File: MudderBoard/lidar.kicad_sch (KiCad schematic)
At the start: 24 parts, among them Q1 NMOS, Q2 NMOS, U1 LM5122QMH/NOPB

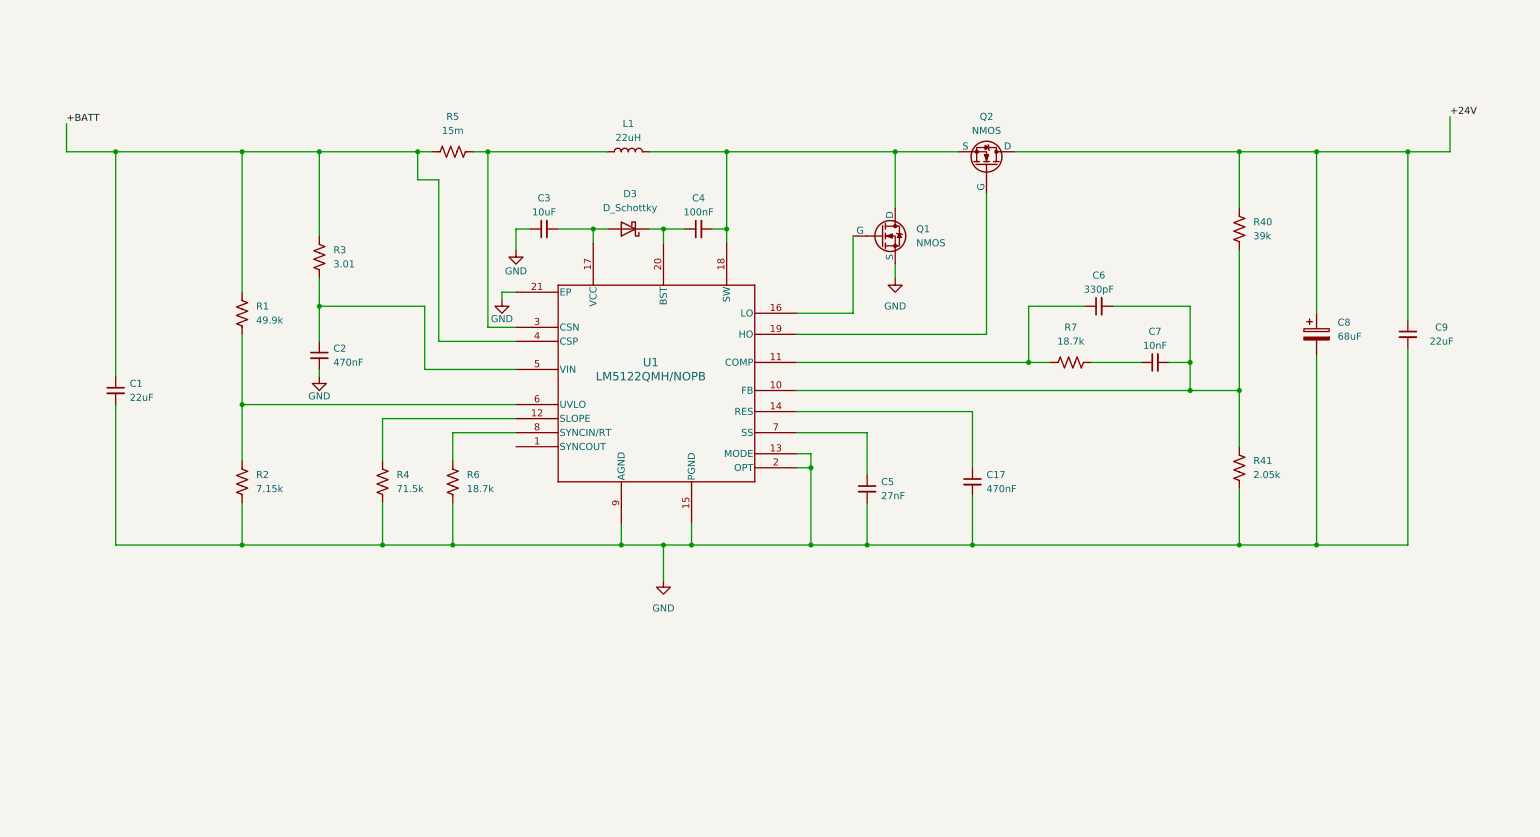
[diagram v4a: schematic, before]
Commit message: added lidar footprints
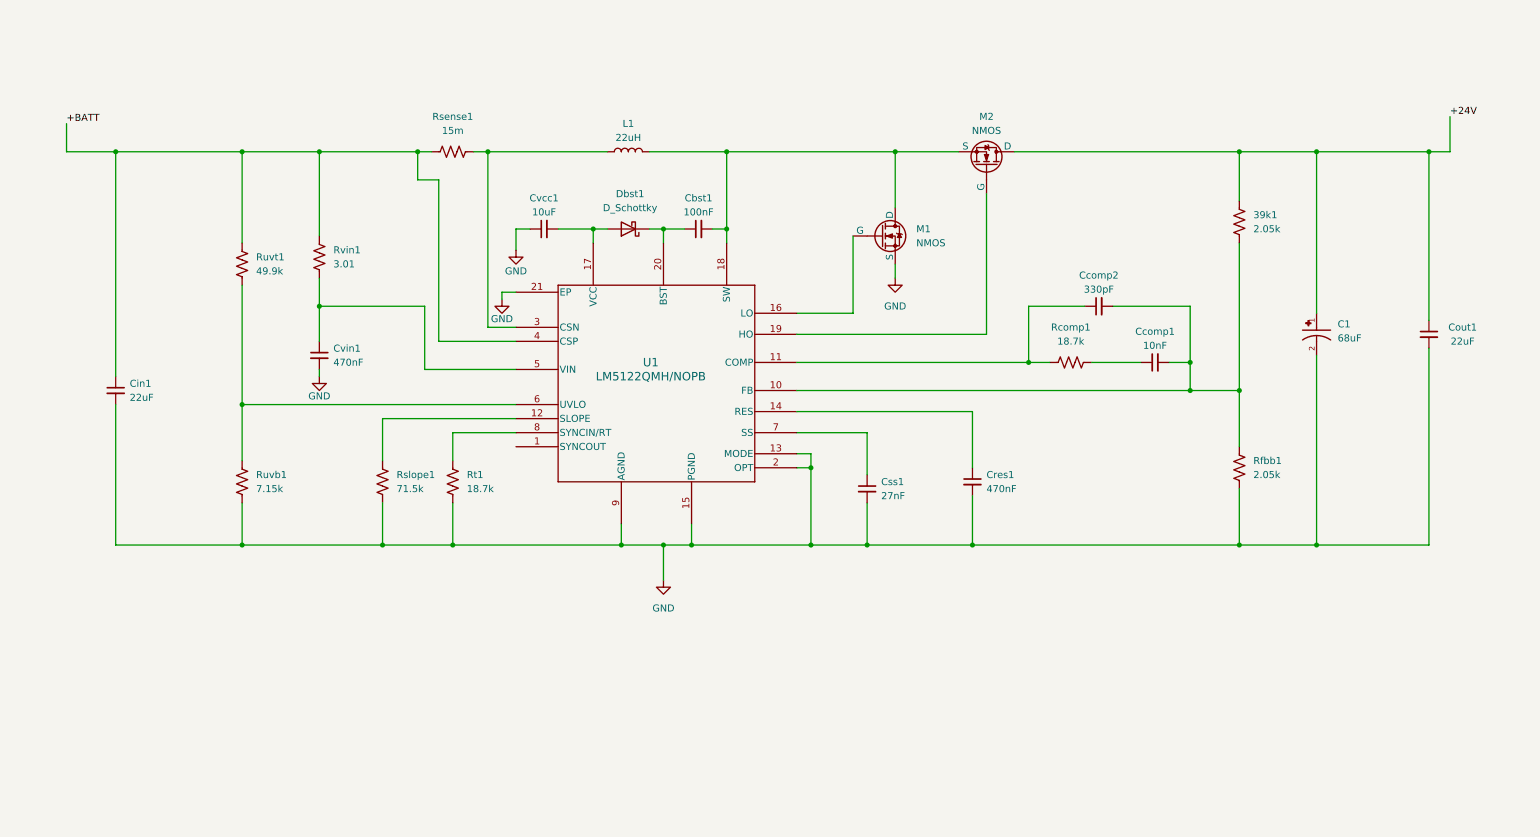
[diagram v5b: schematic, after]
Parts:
- removed C8: 68uF, symbol Device:C_Polarized
- removed R1: 49.9k, symbol Device:R_US
- removed R40: 39k, symbol Device:R_US
- added 39k1: 2.05k, Lidar_Foot:RESC1607X60N, symbol Device:R_US
- added C1: 68uF, EEHZA1V680XP:CAP_EEHZA1V680XP, symbol EEHZA1V680XP:EEHZA1V680XP
- added Ruvt1: 49.9k, Lidar_Foot:RESC1005X40N, symbol Device:R_US
- Cbst1: renamed from C4; footprint (none) -> Lidar_Foot:CAPC2012X88N
- Ccomp1: renamed from C7; footprint (none) -> Lidar_Foot:CAPC2012X75N
- Ccomp2: renamed from C6; footprint (none) -> Lidar_Foot:CAPC0603X33N
- Cin1: renamed from C1; footprint (none) -> Lidar_Foot:CAPC3216X180N
- Cout1: renamed from C9; footprint (none) -> Lidar_Foot:CAPC2012X145N
- Cres1: renamed from C17; footprint (none) -> Lidar_Foot:CAPC2012X95N
- Css1: renamed from C5; footprint (none) -> Lidar_Foot:CAPC1005X55N
- Cvcc1: renamed from C3; footprint (none) -> Lidar_Foot:CAPC2012X135N
- Cvin1: renamed from C2; footprint (none) -> Lidar_Foot:CAPC1608X90N
- Dbst1: renamed from D3; footprint (none) -> Lidar_Foot:DIOM4325X250N
- Rcomp1: renamed from R7; footprint (none) -> Lidar_Foot:RESC0603X26N
- Rfbb1: renamed from R41; footprint (none) -> Lidar_Foot:RESC1005X40N
- Rsense1: renamed from R5; footprint (none) -> Lidar_Foot:RESC3015X65N
- Rslope1: renamed from R4; footprint (none) -> Lidar_Foot:RESC1005X40N
- Rt1: renamed from R6; footprint (none) -> Lidar_Foot:RESC0603X26N
- Ruvb1: renamed from R2; footprint (none) -> Lidar_Foot:RESC1005X40N
- Rvin1: renamed from R3; footprint (none) -> Lidar_Foot:RESC1508X50N
- renumbered Q1 to M1, Q2 to M2
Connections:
- net +24V: now also 39k1.1, C1.1
- net +BATT: now also Ruvt1.1
- net GND: now also C1.2
- net at Ccomp1.2, Ccomp2.2, Rfbb1.1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: now also 39k1.2
- net at Ruvb1.1, U1.6 (UVLO): now also Ruvt1.2
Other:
- moved on the sheet: Cout1

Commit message: Imported footprints to layout
Colin - Make note of these

C30,C32 are generic 0805 caps
L4,L5 are basic insuctors, will need to change when we figure this situation out!

U8,U9 changed to same boost IC as Lidar - these are the same right?
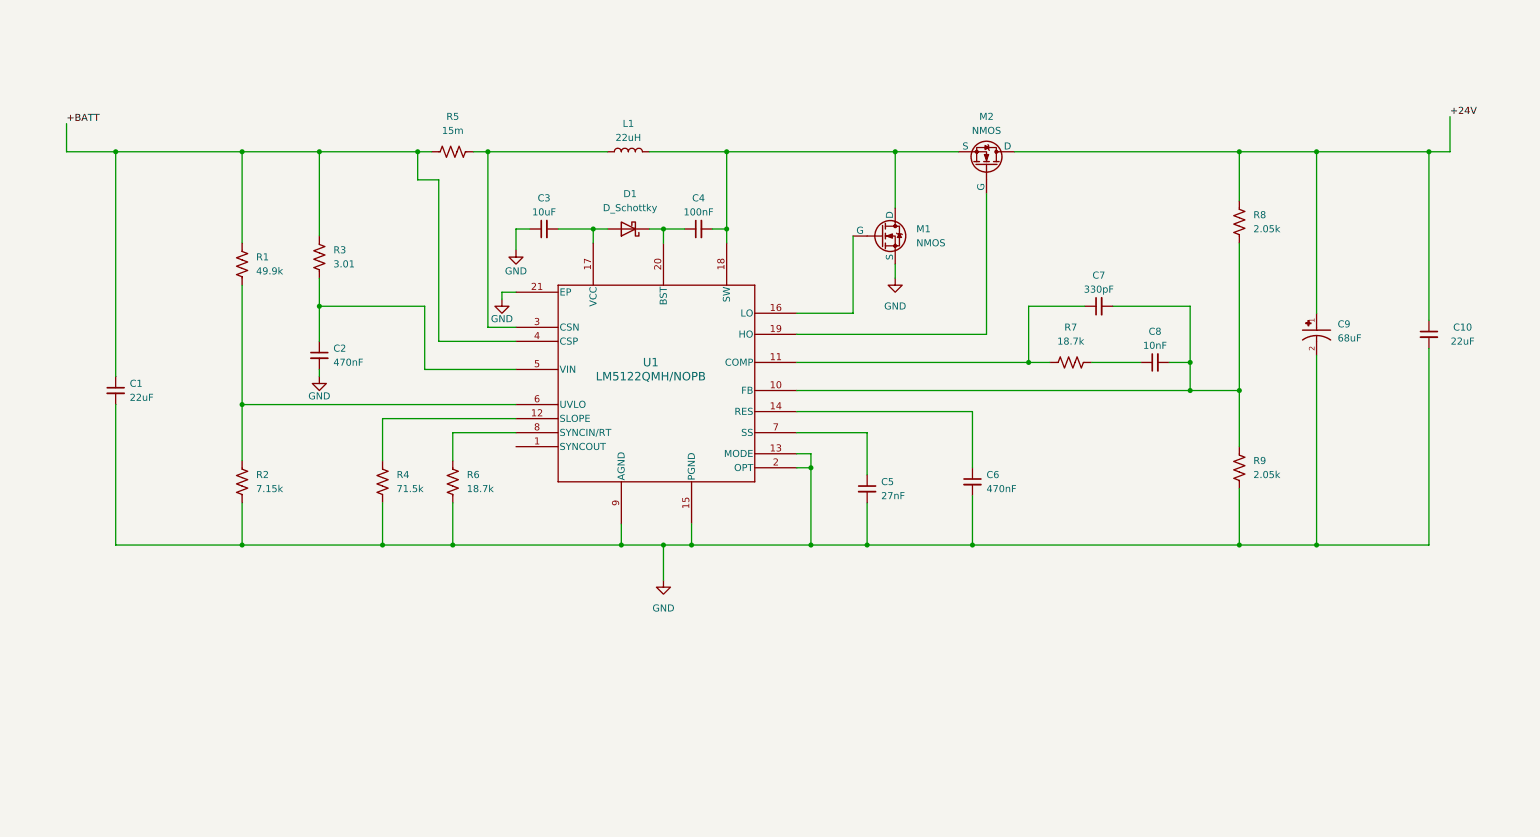
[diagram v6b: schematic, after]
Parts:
- C9: renamed from C1; footprint EEHZA1V680XP:CAP_EEHZA1V680XP -> Lidar_Foot:CAP_EEHZA1V680XP
- renumbered Cin1 to C1, Cout1 to C10, Cvin1 to C2, Cvcc1 to C3, Cbst1 to C4, Css1 to C5, Cres1 to C6, Ccomp2 to C7, Ccomp1 to C8, Dbst1 to D1, Ruvt1 to R1, Ruvb1 to R2, Rvin1 to R3, Rslope1 to R4, Rsense1 to R5, Rt1 to R6, Rcomp1 to R7, 39k1 to R8, Rfbb1 to R9
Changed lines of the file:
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@@
 		(on_board yes)
 		(dnp no)
-		(property "Reference" "Cout1"
+		(property "Reference" "C10"
 			(at 274.066 81.28 0)
 			(effects
@@
 			(project "MudderBoard"
 				(path "/cdf98bf7-80ce-4b13-b655-e6c7c589c122/86bd7edb-9c3d-421e-84f7-984954447f61"
-					(reference "Cout1")
+					(reference "C10")
 					(unit 1)
 				)
@@
 		(dnp no)
 		(fields_autoplaced yes)
-		(property "Reference" "Rt1"
+		(property "Reference" "R6"
 			(at 93.98 107.9499 0)
 			(effects
@@
 			(project "MudderBoard"
 				(path "/cdf98bf7-80ce-4b13-b655-e6c7c589c122/86bd7edb-9c3d-421e-84f7-984954447f61"
-					(reference "Rt1")
+					(reference "R6")
 					(unit 1)
 				)
@@
 		(dnp no)
 		(fields_autoplaced yes)
-		(property "Reference" "Css1"
+		(property "Reference" "C5"
 			(at 168.91 109.2262 0)
 			(effects
@@
 			(project "MudderBoard"
 				(path "/cdf98bf7-80ce-4b13-b655-e6c7c589c122/86bd7edb-9c3d-421e-84f7-984954447f61"
-					(reference "Css1")
+					(reference "C5")
 					(unit 1)
 				)
@@
 		(dnp no)
 		(fields_autoplaced yes)
-		(property "Reference" "Rslope1"
+		(property "Reference" "R4"
 			(at 81.28 107.9499 0)
 			(effects
@@
 			(project "MudderBoard"
 				(path "/cdf98bf7-80ce-4b13-b655-e6c7c589c122/86bd7edb-9c3d-421e-84f7-984954447f61"
-					(reference "Rslope1")
+					(reference "R4")
 					(unit 1)
 				)
@@
 		(dnp no)
 		(fields_autoplaced yes)
-		(property "Reference" "C1"
+		(property "Reference" "C9"
 			(at 251.46 80.7065 90)
 			(effects
@@
 			)
 		)
-		(property "Footprint" "EEHZA1V680XP:CAP_EEHZA1V680XP"
+		(property "Footprint" "Lidar_Foot:CAP_EEHZA1V680XP"
 			(at 247.65 81.28 0)
 			(effects
@@
 			(project "MudderBoard"
 				(path "/cdf98bf7-80ce-4b13-b655-e6c7c589c122/86bd7edb-9c3d-421e-84f7-984954447f61"
-					(reference "C1")
+					(reference "C9")
 					(unit 1)
 				)
@@
 		(dnp no)
 		(fields_autoplaced yes)
-		(property "Reference" "39k1"
+		(property "Reference" "R8"
 			(at 236.22 60.9599 0)
 			(effects
@@
 			(project "MudderBoard"
 				(path "/cdf98bf7-80ce-4b13-b655-e6c7c589c122/86bd7edb-9c3d-421e-84f7-984954447f61"
-					(reference "39k1")
+					(reference "R8")
 					(unit 1)
 				)
@@
 		(dnp no)
 		(fields_autoplaced yes)
-		(property "Reference" "Cvin1"
+		(property "Reference" "C2"
 			(at 69.85 85.0962 0)
 			(effects
@@
 			(project "MudderBoard"
 				(path "/cdf98bf7-80ce-4b13-b655-e6c7c589c122/86bd7edb-9c3d-421e-84f7-984954447f61"
-					(reference "Cvin1")
+					(reference "C2")
 					(unit 1)
 				)
@@
 		(dnp no)
 		(fields_autoplaced yes)
-		(property "Reference" "Rcomp1"
+		(property "Reference" "R7"
 			(at 203.2 81.28 90)
 			(effects
@@
 			(project "MudderBoard"
 				(path "/cdf98bf7-80ce-4b13-b655-e6c7c589c122/86bd7edb-9c3d-421e-84f7-984954447f61"
-					(reference "Rcomp1")
+					(reference "R7")
 					(unit 1)
 				)
@@
 		(dnp no)
 		(fields_autoplaced yes)
-		(property "Reference" "Cin1"
+		(property "Reference" "C1"
 			(at 33.02 91.4462 0)
 			(effects
@@
 			(project "MudderBoard"
 				(path "/cdf98bf7-80ce-4b13-b655-e6c7c589c122/86bd7edb-9c3d-421e-84f7-984954447f61"
-					(reference "Cin1")
+					(reference "C1")
 					(unit 1)
 				)
@@
 		(dnp no)
 		(fields_autoplaced yes)
-		(property "Reference" "Ruvt1"
+		(property "Reference" "R1"
 			(at 55.88 68.5799 0)
 			(effects
@@
 			(project "MudderBoard"
 				(path "/cdf98bf7-80ce-4b13-b655-e6c7c589c122/86bd7edb-9c3d-421e-84f7-984954447f61"
-					(reference "Ruvt1")
+					(reference "R1")
 					(unit 1)
 				)
@@
 		(on_board yes)
 		(dnp no)
-		(property "Reference" "Cvcc1"
+		(property "Reference" "C3"
 			(at 107.95 57.912 90)
 			(effects
@@
 			(project "MudderBoard"
 				(path "/cdf98bf7-80ce-4b13-b655-e6c7c589c122/86bd7edb-9c3d-421e-84f7-984954447f61"
-					(reference "Cvcc1")
+					(reference "C3")
 					(unit 1)
 				)
@@
 		(dnp no)
 		(fields_autoplaced yes)
-		(property "Reference" "Ruvb1"
+		(property "Reference" "R2"
 			(at 55.88 107.9499 0)
 			(effects
@@
 			(project "MudderBoard"
 				(path "/cdf98bf7-80ce-4b13-b655-e6c7c589c122/86bd7edb-9c3d-421e-84f7-984954447f61"
-					(reference "Ruvb1")
+					(reference "R2")
 					(unit 1)
 				)
@@
 		(on_board yes)
 		(dnp no)
-		(property "Reference" "Cbst1"
+		(property "Reference" "C4"
 			(at 135.89 57.912 90)
 			(effects
@@
 			(project "MudderBoard"
 				(path "/cdf98bf7-80ce-4b13-b655-e6c7c589c122/86bd7edb-9c3d-421e-84f7-984954447f61"
-					(reference "Cbst1")
+					(reference "C4")
 					(unit 1)
 				)
@@
 		(dnp no)
 		(fields_autoplaced yes)
-		(property "Reference" "Rsense1"
+		(property "Reference" "R5"
 			(at 91.44 43.18 90)
 			(effects
@@
 			(project "MudderBoard"
 				(path "/cdf98bf7-80ce-4b13-b655-e6c7c589c122/86bd7edb-9c3d-421e-84f7-984954447f61"
-					(reference "Rsense1")
+					(reference "R5")
 					(unit 1)
 				)
@@
 		(on_board yes)
 		(dnp no)
-		(property "Reference" "Rvin1"
+		(property "Reference" "R3"
 			(at 69.85 67.31 0)
 			(effects
@@
 			(project "MudderBoard"
 				(path "/cdf98bf7-80ce-4b13-b655-e6c7c589c122/86bd7edb-9c3d-421e-84f7-984954447f61"
-					(reference "Rvin1")
+					(reference "R3")
 					(unit 1)
 				)
@@
 		(dnp no)
 		(fields_autoplaced yes)
-		(property "Reference" "Rfbb1"
+		(property "Reference" "R9"
 			(at 236.22 105.4099 0)
 			(effects
@@
 			(project "MudderBoard"
 				(path "/cdf98bf7-80ce-4b13-b655-e6c7c589c122/86bd7edb-9c3d-421e-84f7-984954447f61"
-					(reference "Rfbb1")
+					(reference "R9")
 					(unit 1)
 				)
@@
 		(dnp no)
 		(fields_autoplaced yes)
-		(property "Reference" "Cres1"
+		(property "Reference" "C6"
 			(at 187.96 107.9562 0)
 			(effects
@@
 			(project "MudderBoard"
 				(path "/cdf98bf7-80ce-4b13-b655-e6c7c589c122/86bd7edb-9c3d-421e-84f7-984954447f61"
-					(reference "Cres1")
+					(reference "C6")
 					(unit 1)
 				)
@@
 		(on_board yes)
 		(dnp no)
-		(property "Reference" "Ccomp2"
+		(property "Reference" "C7"
 			(at 208.28 71.882 90)
 			(effects
@@
 			(project "MudderBoard"
 				(path "/cdf98bf7-80ce-4b13-b655-e6c7c589c122/86bd7edb-9c3d-421e-84f7-984954447f61"
-					(reference "Ccomp2")
+					(reference "C7")
 					(unit 1)
 				)
@@
 		(dnp no)
 		(fields_autoplaced yes)
-		(property "Reference" "Dbst1"
+		(property "Reference" "D1"
 			(at 123.5075 57.15 0)
 			(effects
@@
 			(project "MudderBoard"
 				(path "/cdf98bf7-80ce-4b13-b655-e6c7c589c122/86bd7edb-9c3d-421e-84f7-984954447f61"
-					(reference "Dbst1")
+					(reference "D1")
 					(unit 1)
 				)
@@
 		(on_board yes)
 		(dnp no)
-		(property "Reference" "Ccomp1"
+		(property "Reference" "C8"
 			(at 218.44 82.042 90)
 			(effects
@@
 			(project "MudderBoard"
 				(path "/cdf98bf7-80ce-4b13-b655-e6c7c589c122/86bd7edb-9c3d-421e-84f7-984954447f61"
-					(reference "Ccomp1")
-					(unit 1)
-				)
+					(reference "C8")
+					(unit 1)
+				)
